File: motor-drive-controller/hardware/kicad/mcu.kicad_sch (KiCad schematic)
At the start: 28 parts, among them J2 Conn_01x03_Pin, J3 JTAG, J4 J_HALL, SW1 SW_Push, U1 STM32F405RGT6, U2 CR2032, Y1 AAH-181-8.000MHZ

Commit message: feat(hw09): add EN_GATE control and WAKE signal handling in hardware design
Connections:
- net DRV.EN_GATE: now reaches U1.40 (PC9)
- no-connect marks 25 -> 24
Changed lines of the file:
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@@
-	)
-	(no_connect
-		(at 163.83 93.98)
 	)
 	(no_connect
@@
 	)
 	(bus_entry
+		(at 179.07 96.52)
+		(size -2.54 -2.54)
+		(stroke
+			(width 0)
+			(type default)
+		)
+	)
+	(bus_entry
 		(at 179.07 81.28)
 		(size -2.54 -2.54)
@@
 		)
 	)
+	(bus
+		(pts
+			(xy 179.07 101.6) (xy 184.15 101.6)
+		)
+		(stroke
+			(width 0)
+			(type default)
+		)
+	)
 	(wire
 		(pts
@@
 		)
 	)
+	(bus
+		(pts
+			(xy 179.07 96.52) (xy 179.07 101.6)
+		)
+		(stroke
+			(width 0)
+			(type default)
+		)
+	)
 	(wire
 		(pts
@@
 		(pts
 			(xy 212.09 39.37) (xy 212.09 33.02)
+		)
+		(stroke
+			(width 0)
+			(type default)
+		)
+	)
+	(wire
+		(pts
+			(xy 163.83 93.98) (xy 176.53 93.98)
 		)
 		(stroke
@@
 			)
 			(justify left bottom)
+		)
+	)
+	(label "DRV.EN_GATE"
+		(at 176.53 93.98 180)
+		(effects
+			(font
+				(size 1.27 1.27)
+			)
+			(justify right bottom)
 		)
 	)
@@
 		)
 	)
+	(hierarchical_label "DRV{CTRL}"
+		(shape output)
+		(at 184.15 101.6 0)
+		(effects
+			(font
+				(size 1.27 1.27)
+			)
+			(justify left)
+		)
+	)

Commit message: fix(hw09): fix ERC issues
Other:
- note added: "Розв'язувальні конденсатори і живлення MCU"
- note removed: "Розв'язувальні конденсатори"

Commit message: feat(hw09): update footprint properties for components in schematic files
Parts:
- C10, C11, C8, C9: footprint (none) -> Capacitor_SMD:C_0805_2012Metric
- C12, C13, C14, C15, C22, C3, C4, C5, C6, C7: footprint (none) -> Capacitor_SMD:C_0603_1608Metric
- J2: footprint (none) -> Connector_PinHeader_2.54mm:PinHeader_1x03_P2.54mm_Vertical
- J3: footprint (none) -> Connector_IDC:IDC-Header_2x10_P2.54mm_Vertical
- J4: footprint (none) -> Connector_PinHeader_2.54mm:PinHeader_1x05_P2.54mm_Vertical
- R11, R13, R14, R17, R18, R19: footprint (none) -> Resistor_SMD:R_0603_1608Metric
- SW1: footprint (none) -> Button_Switch_SMD:SW_SPST_TL3342
- U2: footprint (none) -> CR2032:CR2032-SMD
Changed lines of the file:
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@@
 			)
 		)
-		(property "Footprint" ""
+		(property "Footprint" "Capacitor_SMD:C_0805_2012Metric"
 			(at 105.1052 176.53 0)
 			(hide yes)
@@
 			)
 		)
-		(property "Footprint" ""
+		(property "Footprint" "Connector_IDC:IDC-Header_2x10_P2.54mm_Vertical"
 			(at 48.26 82.55 0)
 			(hide yes)
@@
 			)
 		)
-		(property "Footprint" ""
+		(property "Footprint" "Capacitor_SMD:C_0603_1608Metric"
 			(at 229.5652 86.36 0)
 			(hide yes)
@@
 			)
 		)
-		(property "Footprint" ""
+		(property "Footprint" "Resistor_SMD:R_0603_1608Metric"
 			(at 51.562 73.66 90)
 			(hide yes)
@@
 			)
 		)
-		(property "Footprint" ""
+		(property "Footprint" "CR2032:CR2032-SMD"
 			(at 227.33 142.24 0)
 			(hide yes)
@@
 			)
 		)
-		(property "Footprint" ""
+		(property "Footprint" "Capacitor_SMD:C_0603_1608Metric"
 			(at 62.23 119.6848 0)
 			(hide yes)
@@
 			)
 		)
-		(property "Footprint" ""
+		(property "Footprint" "Connector_PinHeader_2.54mm:PinHeader_1x03_P2.54mm_Vertical"
 			(at 215.9 125.73 0)
 			(hide yes)
@@
 			)
 		)
-		(property "Footprint" ""
+		(property "Footprint" "Button_Switch_SMD:SW_SPST_TL3342"
 			(at 217.17 82.55 0)
 			(hide yes)
@@
 			)
 		)
-		(property "Footprint" ""
+		(property "Footprint" "Capacitor_SMD:C_0603_1608Metric"
 			(at 48.26 117.1448 0)
 			(hide yes)
@@
 			)
 		)
-		(property "Footprint" ""
+		(property "Footprint" "Capacitor_SMD:C_0603_1608Metric"
 			(at 54.61 124.7648 0)
 			(hide yes)
@@
 			)
 		)
-		(property "Footprint" ""
+		(property "Footprint" "Capacitor_SMD:C_0805_2012Metric"
 			(at 40.64 106.9848 0)
 			(hide yes)
@@
 			)
 		)
-		(property "Footprint" ""
+		(property "Footprint" "Capacitor_SMD:C_0603_1608Metric"
 			(at 75.8952 176.53 0)
 			(hide yes)
@@
 			)
 		)
-		(property "Footprint" ""
+		(property "Footprint" "Resistor_SMD:R_0603_1608Metric"
 			(at 164.338 172.72 90)
 			(hide yes)
@@
 			)
 		)
-		(property "Footprint" ""
+		(property "Footprint" "Resistor_SMD:R_0603_1608Metric"
 			(at 154.178 172.72 90)
 			(hide yes)
@@
 			)
 		)
-		(property "Footprint" ""
+		(property "Footprint" "Resistor_SMD:R_0603_1608Metric"
 			(at 60.452 73.66 90)
 			(hide yes)
@@
 			)
 		)
-		(property "Footprint" ""
+		(property "Footprint" "Resistor_SMD:R_0603_1608Metric"
 			(at 243.332 83.82 90)
 			(hide yes)
@@
 			)
 		)
-		(property "Footprint" ""
+		(property "Footprint" "Capacitor_SMD:C_0603_1608Metric"
 			(at 247.3452 48.26 0)
 			(hide yes)
@@
 			)
 		)
-		(property "Footprint" ""
+		(property "Footprint" "Capacitor_SMD:C_0603_1608Metric"
 			(at 240.9952 144.78 0)
 			(hide yes)
@@
 			)
 		)
-		(property "Footprint" ""
+		(property "Footprint" "Capacitor_SMD:C_0603_1608Metric"
 			(at 40.64 122.2248 0)
 			(hide yes)
@@
 			)
 		)
-		(property "Footprint" ""
+		(property "Footprint" "Capacitor_SMD:C_0603_1608Metric"
 			(at 105.41 38.4048 0)
 			(hide yes)
@@
 			)
 		)
-		(property "Footprint" ""
+		(property "Footprint" "Capacitor_SMD:C_0603_1608Metric"
 			(at 213.0552 49.53 0)
 			(hide yes)
@@
 			)
 		)
-		(property "Footprint" ""
+		(property "Footprint" "Resistor_SMD:R_0603_1608Metric"
 			(at 69.342 73.66 90)
 			(hide yes)
@@
 			)
 		)
-		(property "Footprint" ""
+		(property "Footprint" "Capacitor_SMD:C_0805_2012Metric"
 			(at 64.4652 176.53 0)
 			(hide yes)
@@
 			)
 		)
-		(property "Footprint" ""
+		(property "Footprint" "Connector_PinHeader_2.54mm:PinHeader_1x05_P2.54mm_Vertical"
 			(at 83.82 48.26 0)
 			(hide yes)
@@
 			)
 		)
-		(property "Footprint" ""
+		(property "Footprint" "Capacitor_SMD:C_0805_2012Metric"
 			(at 117.8052 176.53 0)
 			(hide yes)

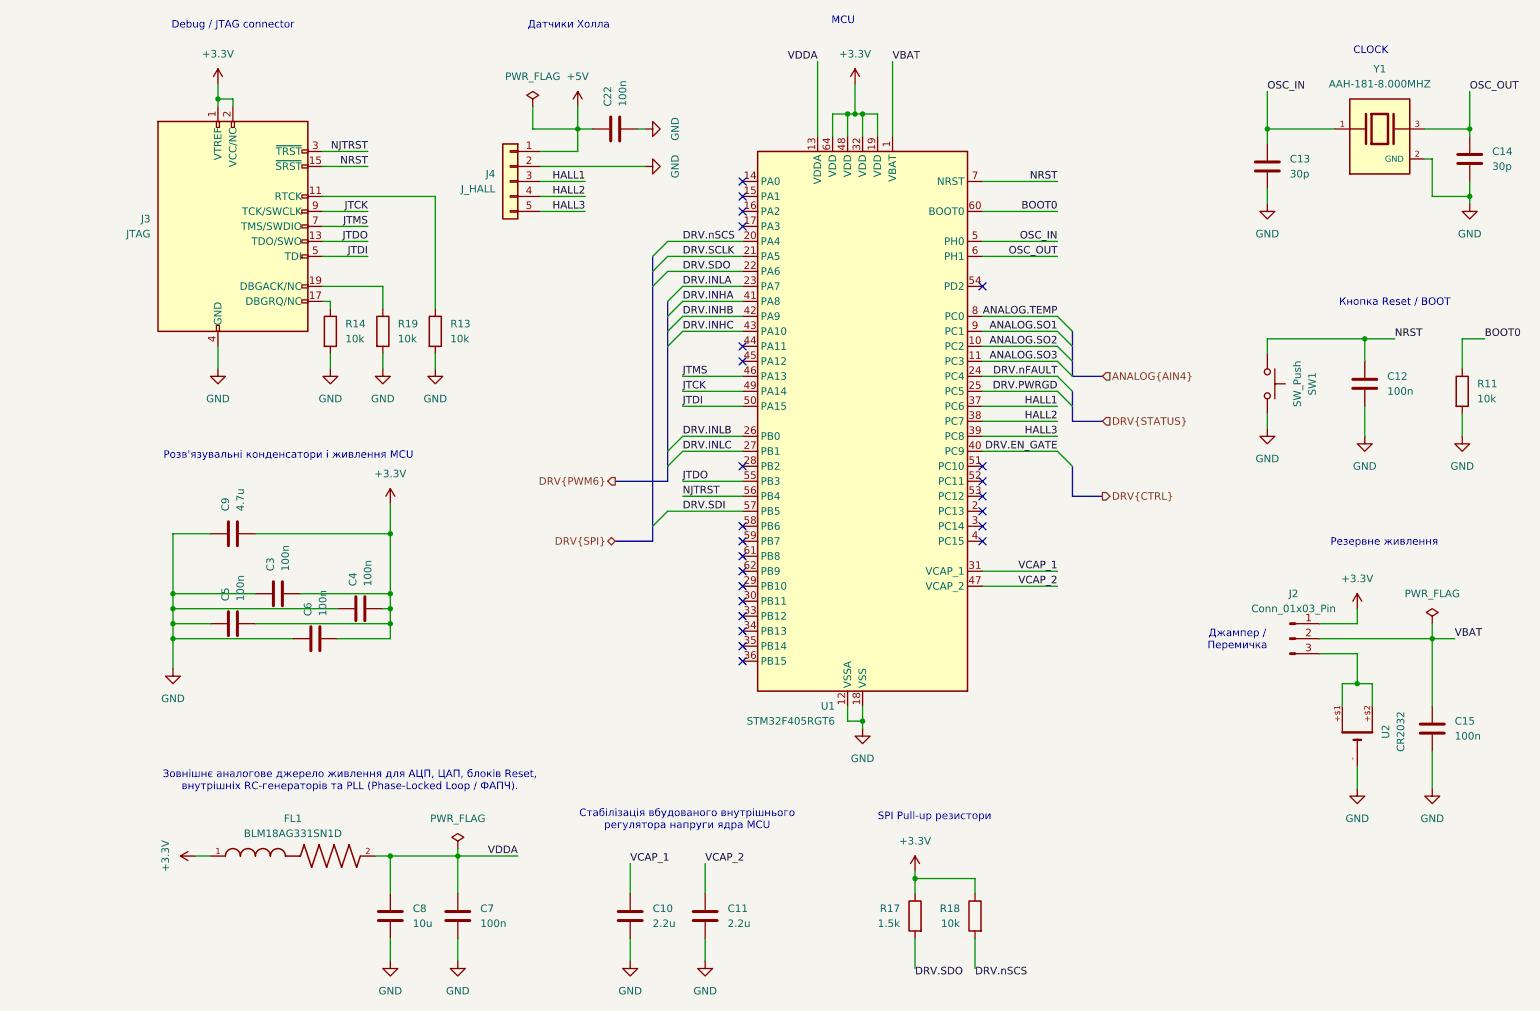
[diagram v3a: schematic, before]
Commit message: feat(hw09): add WAKE control signal
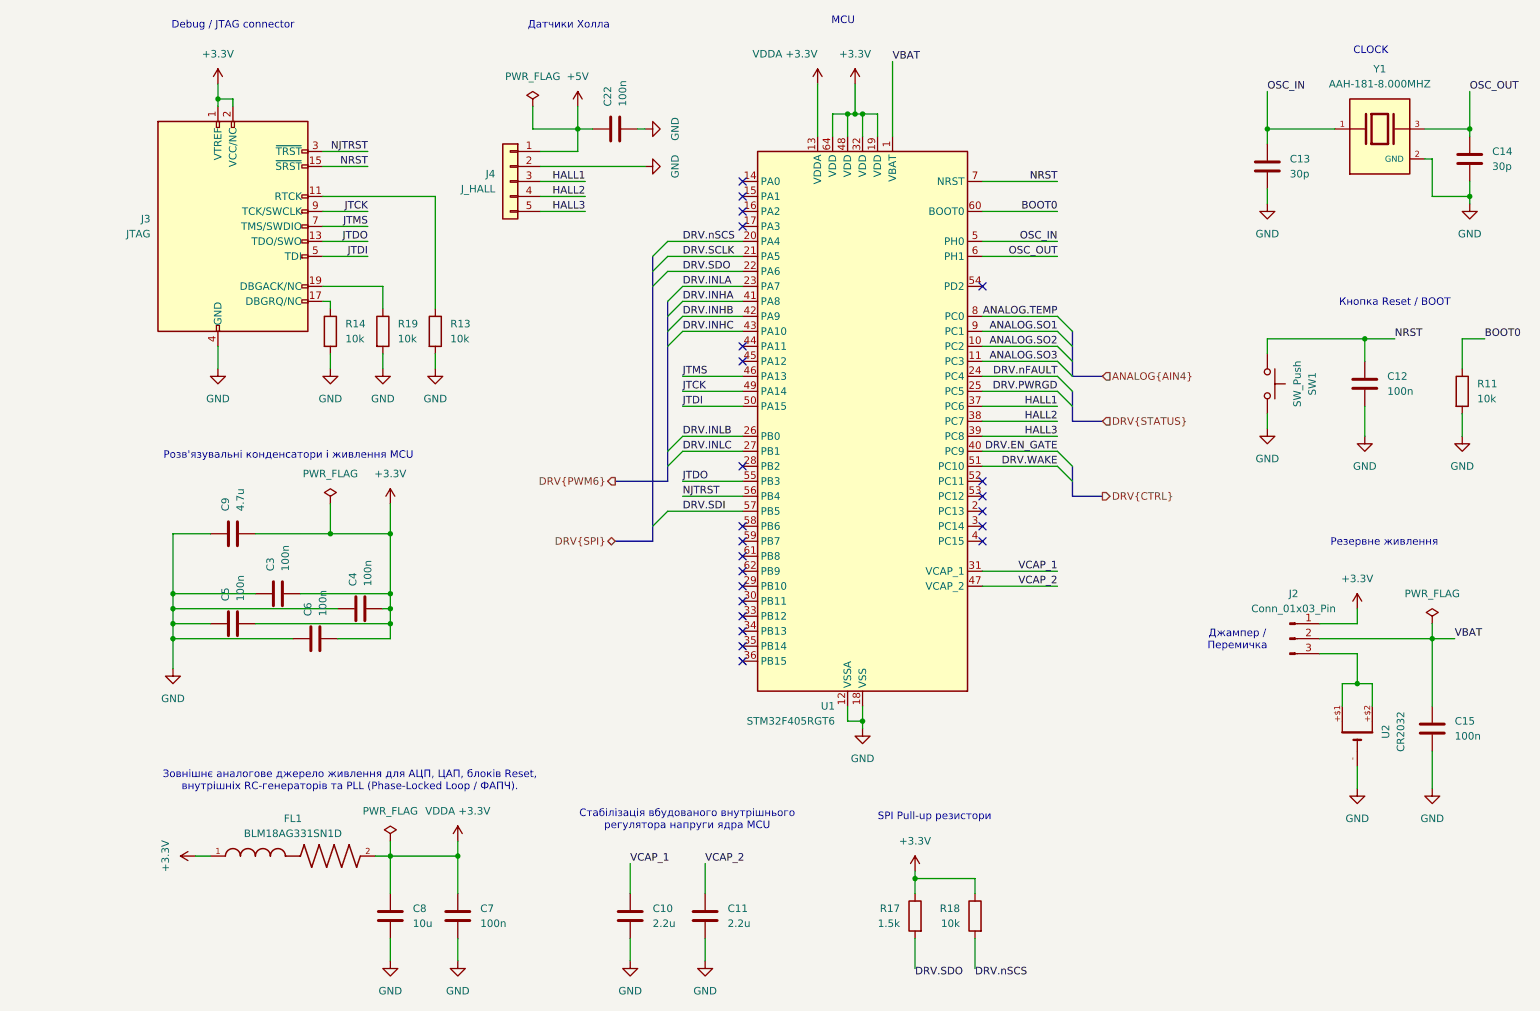
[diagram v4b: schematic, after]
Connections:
- net DRV.WAKE: now reaches U1.51 (PC10)
- net VDDA renamed VDDA +3.3V
- no-connect marks 24 -> 23
